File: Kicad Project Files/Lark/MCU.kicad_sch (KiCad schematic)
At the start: 19 parts, among them J9 0530470410, U16 STM32H743VIT6, Y1 8Mhz

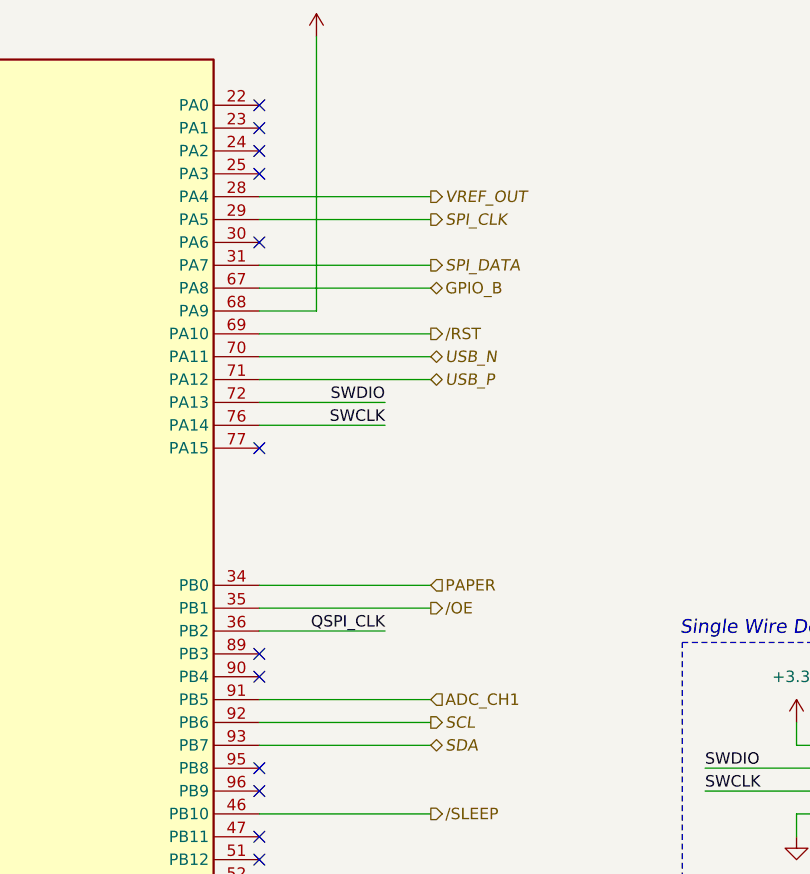
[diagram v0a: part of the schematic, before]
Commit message: fixed issue with ADC, Rev-ed board.
Turns out, you can in fact set PB5 to analog, but its use is with I2C1_SMBA, not the ADC, So I changed it to pin PA3. This renders the head temp functionality on revision 01.00.1 null.
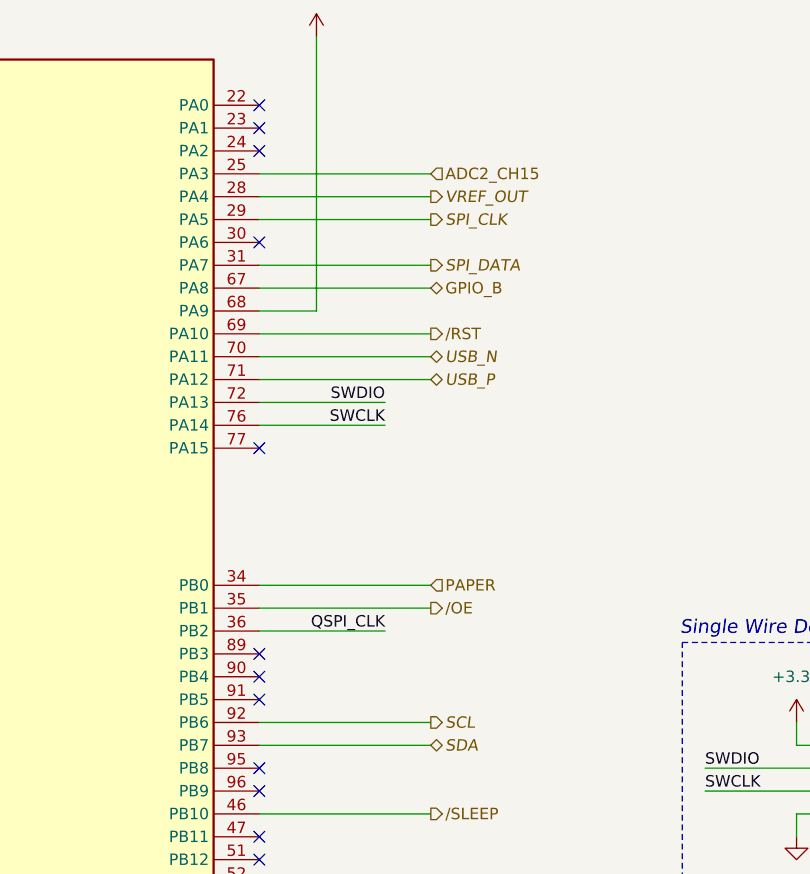
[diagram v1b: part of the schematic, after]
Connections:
- net ADC2_CH15: now reaches U16.25 (PA3)
- net ADC_CH1: no longer names the net of U16.91 (PB5)
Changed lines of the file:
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@@
 		(title "Lark Print Engine")
 		(date "2025-10-08")
-		(rev "01.00.01")
+		(rev "01.00.02")
 		(comment 1 "Thermal Print Engine")
 		(comment 2 "Designer: HamSlices")
@@
 	)
 	(no_connect
+		(at 130.81 97.79)
+	)
+	(no_connect
 		(at 130.81 115.57)
 	)
@@
 	)
 	(no_connect
-		(at 130.81 39.37)
-	)
-	(no_connect
 		(at 85.09 73.66)
 	)
@@
 	(wire
 		(pts
-			(xy 130.81 97.79) (xy 149.86 97.79)
-		)
-		(stroke
-			(width 0)
-			(type default)
-		)
-	)
-	(wire
-		(pts
 			(xy 256.54 100.33) (xy 267.97 100.33)
 		)
@@
 	(wire
 		(pts
+			(xy 130.81 39.37) (xy 149.86 39.37)
+		)
+		(stroke
+			(width 0)
+			(type default)
+		)
+	)
+	(wire
+		(pts
 			(xy 267.97 41.91) (xy 267.97 44.45)
 		)
@@
 		)
 	)
-	(hierarchical_label "ADC_CH1"
+	(hierarchical_label "ADC2_CH15"
 		(shape input)
-		(at 149.86 97.79 0)
+		(at 149.86 39.37 0)
 		(effects
 			(font
